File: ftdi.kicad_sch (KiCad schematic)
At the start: 31 parts, among them U1001 AT93C56, U1002 FT2232HL, Y1001 12MHz

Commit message: Schematic sketching done
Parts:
- R1001, R1002, R1005, R1006, R1007, R1008, R1009, R1010, R1011: Tolerance (none) -> 5%
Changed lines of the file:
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@@
+      (effects (font (size 1.27 1.27)) hide)
+    )
+    (property "Tolerance" "5%" (id 4) (at 38.1 44.45 0)
       (effects (font (size 1.27 1.27)) hide)
     )
@@
     )
     (property "Datasheet" "~" (id 3) (at 38.1 57.15 0)
+      (effects (font (size 1.27 1.27)) hide)
+    )
+    (property "Tolerance" "5%" (id 4) (at 38.1 57.15 0)
       (effects (font (size 1.27 1.27)) hide)
     )
@@
       (effects (font (size 1.27 1.27)) hide)
     )
+    (property "Tolerance" "5%" (id 4) (at 83.82 123.19 0)
+      (effects (font (size 1.27 1.27)) hide)
+    )
     (pin "1")
     (pin "2")
@@
       (effects (font (size 1.27 1.27)) hide)
     )
+    (property "Tolerance" "5%" (id 4) (at 83.82 101.6 0)
+      (effects (font (size 1.27 1.27)) hide)
+    )
     (pin "1")
     (pin "2")
@@
     )
     (property "Datasheet" "~" (id 3) (at 91.44 101.6 0)
+      (effects (font (size 1.27 1.27)) hide)
+    )
+    (property "Tolerance" "5%" (id 4) (at 91.44 101.6 0)
       (effects (font (size 1.27 1.27)) hide)
     )
@@
       (effects (font (size 1.27 1.27)) hide)
     )
+    (property "Tolerance" "5%" (id 4) (at 101.6 96.52 0)
+      (effects (font (size 1.27 1.27)) hide)
+    )
     (pin "1")
     (pin "2")
@@
     )
     (property "Datasheet" "~" (id 3) (at 95.25 85.09 0)
+      (effects (font (size 1.27 1.27)) hide)
+    )
+    (property "Tolerance" "5%" (id 4) (at 95.25 85.09 0)
       (effects (font (size 1.27 1.27)) hide)
     )
@@
       (effects (font (size 1.27 1.27)) hide)
     )
+    (property "Tolerance" "5%" (id 4) (at 76.2 101.6 0)
+      (effects (font (size 1.27 1.27)) hide)
+    )
     (pin "1")
     (pin "2")
@@
       (effects (font (size 1.27 1.27)) hide)
     )
+    (property "Tolerance" "5%" (id 4) (at 177.8 125.73 0)
+      (effects (font (size 1.27 1.27)) hide)
+    )

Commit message: Update schematic layout, separate into sheets
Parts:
- renumbered C1001 to C1301, C1002 to C1302, C1003 to C1303, C1004 to C1304, C1005 to C1305, C1006 to C1306, C1007 to C1307, C1008 to C1308, C1009 to C1309, C1010 to C1310, C1011 to C1311, C1012 to C1312, C1013 to C1313, C1014 to C1314, D1001 to D1301, FB1001 to FB1301, FB1002 to FB1302, R1001 to R1301, R1002 to R1302, R1003 to R1303, R1004 to R1304, R1005 to R1305, R1006 to R1306, R1007 to R1307, R1008 to R1308, R1009 to R1309, R1010 to R1310, R1011 to R1311, U1001 to U1301, U1002 to U1302, Y1001 to Y1301
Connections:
- net CDONE renamed IOB.CDONE
- net IO1 renamed IOB.IO1
- net IO2 renamed IOB.IO2
- net ~{CRESET} renamed IOB.~{CRESET}

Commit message: Schematic update
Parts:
- C1301, C1302: Spec1 (none) -> 25V; Spec2 (none) -> C0G; Tolerance (none) -> 10%
- C1303, C1304, C1305, C1306, C1307, C1308, C1309, C1310, C1311, C1312, C1313, C1314: Spec1 (none) -> 16V; Spec2 (none) -> X5R; Tolerance (none) -> 20%
- R1307: value 2.2k -> 2.4k
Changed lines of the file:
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@@
+      (effects (font (size 1.27 1.27)) hide)
+    )
+    (property "Spec1" "16V" (id 4) (at 254 76.2 0)
+      (effects (font (size 1.27 1.27)) hide)
+    )
+    (property "Spec2" "X5R" (id 5) (at 254 76.2 0)
+      (effects (font (size 1.27 1.27)) hide)
+    )
+    (property "Tolerance" "20%" (id 6) (at 254 76.2 0)
       (effects (font (size 1.27 1.27)) hide)
     )
@@
     )
     (property "Datasheet" "~" (id 3) (at 241.3 76.2 0)
+      (effects (font (size 1.27 1.27)) hide)
+    )
+    (property "Spec1" "16V" (id 4) (at 241.3 76.2 0)
+      (effects (font (size 1.27 1.27)) hide)
+    )
+    (property "Spec2" "X5R" (id 5) (at 241.3 76.2 0)
+      (effects (font (size 1.27 1.27)) hide)
+    )
+    (property "Tolerance" "20%" (id 6) (at 241.3 76.2 0)
       (effects (font (size 1.27 1.27)) hide)
     )
@@
       (effects (font (size 1.27 1.27)) hide)
     )
+    (property "Spec1" "16V" (id 4) (at 266.7 44.45 0)
+      (effects (font (size 1.27 1.27)) hide)
+    )
+    (property "Spec2" "X5R" (id 5) (at 266.7 44.45 0)
+      (effects (font (size 1.27 1.27)) hide)
+    )
+    (property "Tolerance" "20%" (id 6) (at 266.7 44.45 0)
+      (effects (font (size 1.27 1.27)) hide)
+    )
     (pin "1")
     (pin "2")
@@
     )
     (property "Datasheet" "~" (id 3) (at 241.3 139.7 0)
+      (effects (font (size 1.27 1.27)) hide)
+    )
+    (property "Spec1" "16V" (id 4) (at 241.3 139.7 0)
+      (effects (font (size 1.27 1.27)) hide)
+    )
+    (property "Spec2" "X5R" (id 5) (at 241.3 139.7 0)
+      (effects (font (size 1.27 1.27)) hide)
+    )
+    (property "Tolerance" "20%" (id 6) (at 241.3 139.7 0)
       (effects (font (size 1.27 1.27)) hide)
     )
@@
       (effects (font (size 1.27 1.27)) hide)
     )
+    (property "Spec1" "16V" (id 4) (at 241.3 44.45 0)
+      (effects (font (size 1.27 1.27)) hide)
+    )
+    (property "Spec2" "X5R" (id 5) (at 241.3 44.45 0)
+      (effects (font (size 1.27 1.27)) hide)
+    )
+    (property "Tolerance" "20%" (id 6) (at 241.3 44.45 0)
+      (effects (font (size 1.27 1.27)) hide)
+    )
     (pin "1")
     (pin "2")
@@
     )
     (property "Datasheet" "~" (id 3) (at 76.2 151.13 0)
+      (effects (font (size 1.27 1.27)) hide)
+    )
+    (property "Spec1" "25V" (id 4) (at 76.2 151.13 0)
+      (effects (font (size 1.27 1.27)) hide)
+    )
+    (property "Spec2" "C0G" (id 5) (at 76.2 151.13 0)
+      (effects (font (size 1.27 1.27)) hide)
+    )
+    (property "Tolerance" "10%" (id 6) (at 76.2 151.13 0)
       (effects (font (size 1.27 1.27)) hide)
     )
@@
       (effects (font (size 1.27 1.27)) hide)
     )
+    (property "Spec1" "16V" (id 4) (at 254 139.7 0)
+      (effects (font (size 1.27 1.27)) hide)
+    )
+    (property "Spec2" "X5R" (id 5) (at 254 139.7 0)
+      (effects (font (size 1.27 1.27)) hide)
+    )
+    (property "Tolerance" "20%" (id 6) (at 254 139.7 0)
+      (effects (font (size 1.27 1.27)) hide)
+    )
     (pin "1")
     (pin "2")
@@
     (in_bom yes) (on_board yes) (fields_autoplaced)
     (property "Reference" "R1307" (id 0) (at 83.82 126.3555 90))
-    (property "Value" "2.2k" (id 1) (at 83.82 129.1306 90))
+    (property "Value" "2.4k" (id 1) (at 83.82 129.1306 90))
     (property "Footprint" "Resistor_SMD:R_0805_2012Metric" (id 2) (at 83.82 121.412 90)
       (effects (font (size 1.27 1.27)) hide)
@@
     )
     (property "Datasheet" "~" (id 3) (at 228.6 139.7 0)
+      (effects (font (size 1.27 1.27)) hide)
+    )
+    (property "Spec1" "16V" (id 4) (at 228.6 139.7 0)
+      (effects (font (size 1.27 1.27)) hide)
+    )
+    (property "Spec2" "X5R" (id 5) (at 228.6 139.7 0)
+      (effects (font (size 1.27 1.27)) hide)
+    )
+    (property "Tolerance" "20%" (id 6) (at 228.6 139.7 0)
       (effects (font (size 1.27 1.27)) hide)
     )
@@
       (effects (font (size 1.27 1.27)) hide)
     )
+    (property "Spec1" "16V" (id 4) (at 228.6 44.45 0)
+      (effects (font (size 1.27 1.27)) hide)
+    )
+    (property "Spec2" "X5R" (id 5) (at 228.6 44.45 0)
+      (effects (font (size 1.27 1.27)) hide)
+    )
+    (property "Tolerance" "20%" (id 6) (at 228.6 44.45 0)
+      (effects (font (size 1.27 1.27)) hide)
+    )
     (pin "1")
     (pin "2")
@@
       (effects (font (size 1.27 1.27)) hide)
     )
+    (property "Spec1" "16V" (id 4) (at 254 107.95 0)
+      (effects (font (size 1.27 1.27)) hide)
+    )
+    (property "Spec2" "X5R" (id 5) (at 254 107.95 0)
+      (effects (font (size 1.27 1.27)) hide)
+    )
+    (property "Tolerance" "20%" (id 6) (at 254 107.95 0)
+      (effects (font (size 1.27 1.27)) hide)
+    )
     (pin "1")
     (pin "2")
@@
     )
     (property "Datasheet" "~" (id 3) (at 266.7 139.7 0)
+      (effects (font (size 1.27 1.27)) hide)
+    )
+    (property "Spec1" "16V" (id 4) (at 266.7 139.7 0)
+      (effects (font (size 1.27 1.27)) hide)
+    )
+    (property "Spec2" "X5R" (id 5) (at 266.7 139.7 0)
+      (effects (font (size 1.27 1.27)) hide)
+    )
+    (property "Tolerance" "20%" (id 6) (at 266.7 139.7 0)
       (effects (font (size 1.27 1.27)) hide)
     )
@@
       (effects (font (size 1.27 1.27)) hide)
     )
+    (property "Spec1" "16V" (id 4) (at 241.3 107.95 0)
+      (effects (font (size 1.27 1.27)) hide)
+    )
+    (property "Spec2" "X5R" (id 5) (at 241.3 107.95 0)
+      (effects (font (size 1.27 1.27)) hide)
+    )
+    (property "Tolerance" "20%" (id 6) (at 241.3 107.95 0)
+      (effects (font (size 1.27 1.27)) hide)
+    )
     (pin "1")
     (pin "2")
@@
       (effects (font (size 1.27 1.27)) hide)
     )
+    (property "Spec1" "25V" (id 4) (at 99.06 151.13 0)
+      (effects (font (size 1.27 1.27)) hide)
+    )
+    (property "Spec2" "C0G" (id 5) (at 99.06 151.13 0)
+      (effects (font (size 1.27 1.27)) hide)
+    )
+    (property "Tolerance" "10%" (id 6) (at 99.06 151.13 0)
+      (effects (font (size 1.27 1.27)) hide)
+    )
     (pin "1")
     (pin "2")
@@
       (effects (font (size 1.27 1.27)) hide)
     )
+    (property "Spec1" "16V" (id 4) (at 254 44.45 0)
+      (effects (font (size 1.27 1.27)) hide)
+    )
+    (property "Spec2" "X5R" (id 5) (at 254 44.45 0)
+      (effects (font (size 1.27 1.27)) hide)
+    )
+    (property "Tolerance" "20%" (id 6) (at 254 44.45 0)
+      (effects (font (size 1.27 1.27)) hide)
+    )

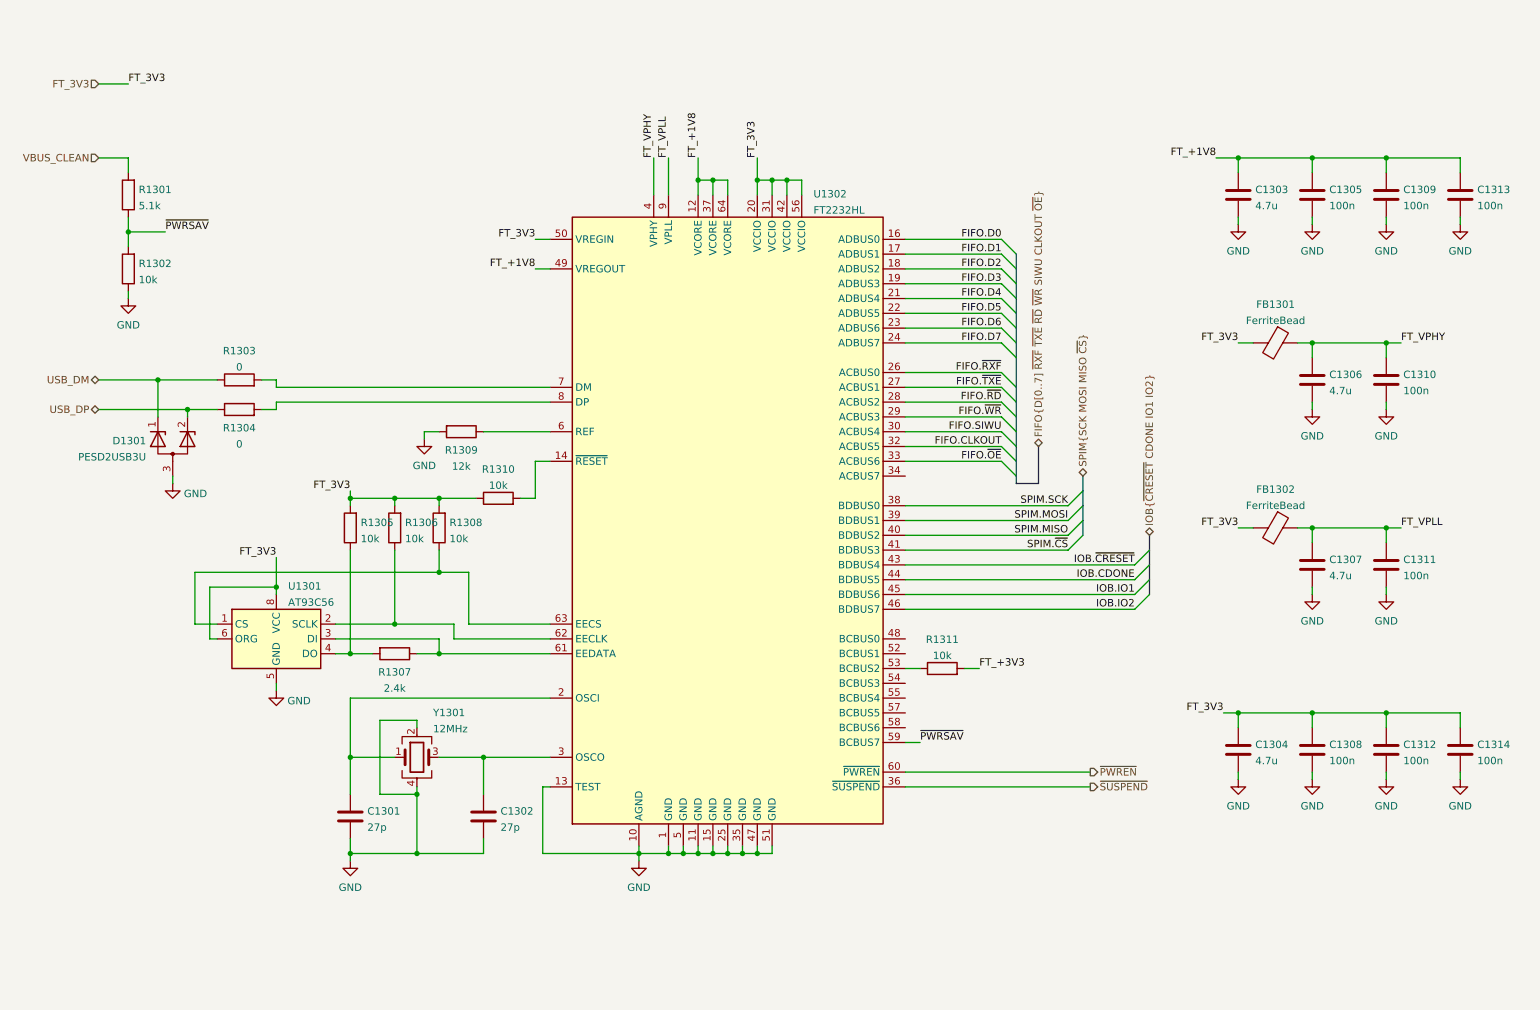
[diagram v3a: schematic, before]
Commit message: Schematic: better LDO output capacitor selection, clarified BOM
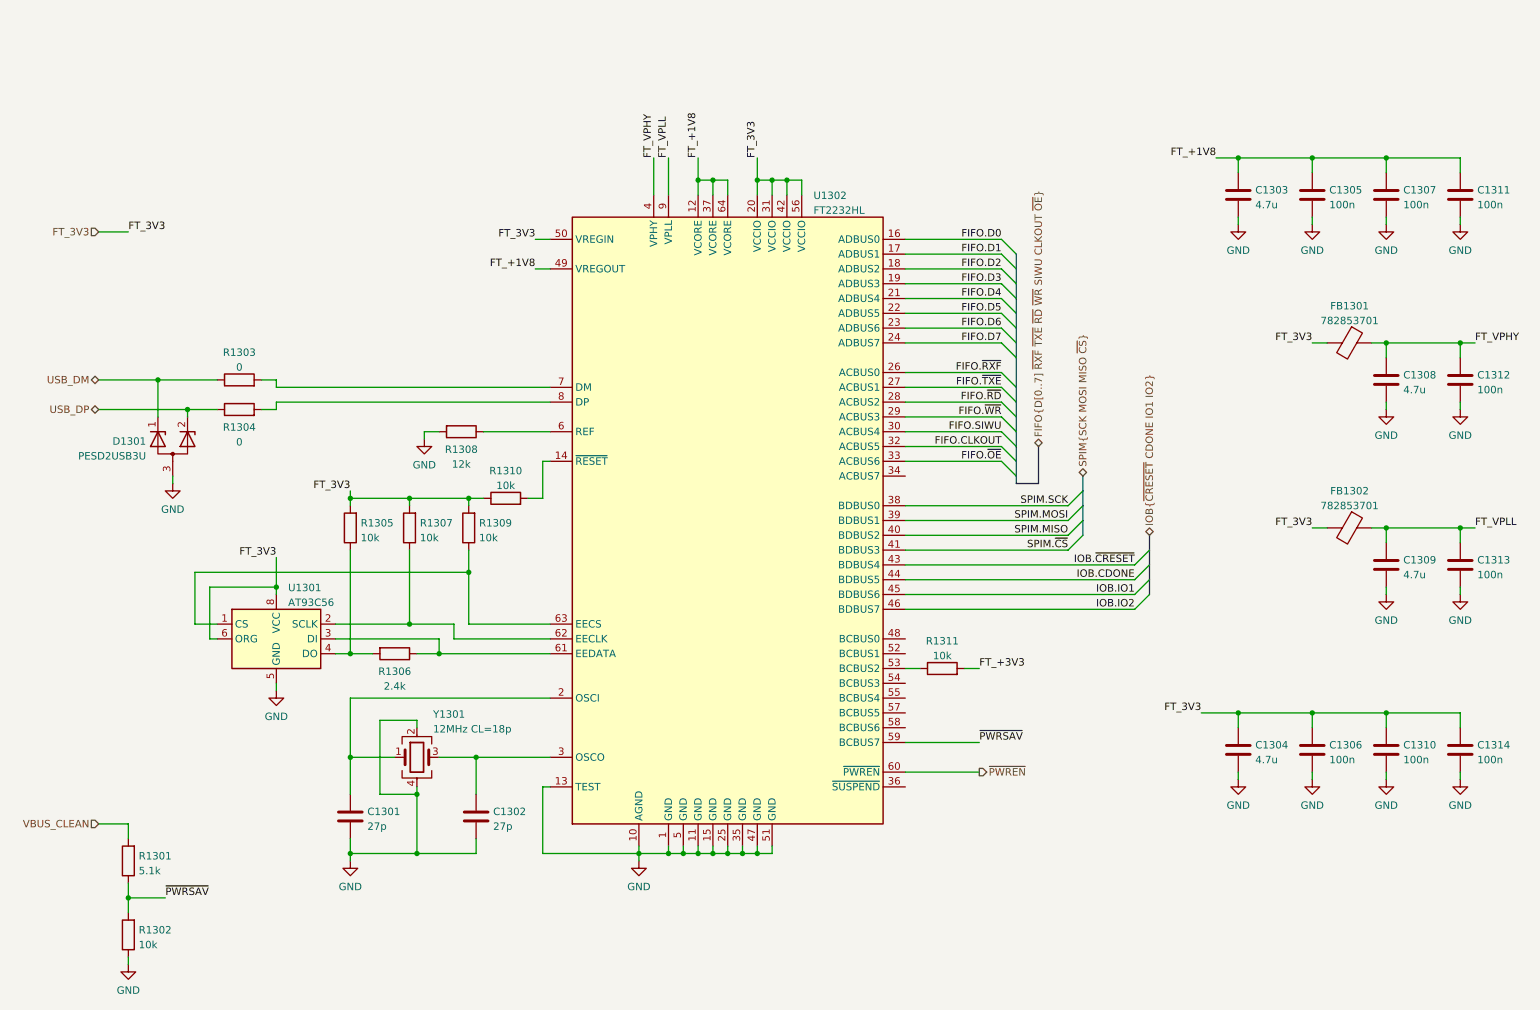
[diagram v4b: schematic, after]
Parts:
- C1303, C1304, C1305, C1314: Spec1 16V -> (none); Spec2 X5R -> (none); Tolerance 20% -> (none)
- C1306: renamed from C1308; Spec1 16V -> (none); Spec2 X5R -> (none); Tolerance 20% -> (none)
- C1307: renamed from C1309; Spec1 16V -> (none); Spec2 X5R -> (none); Tolerance 20% -> (none)
- C1308: renamed from C1306; Spec1 16V -> (none); Spec2 X5R -> (none); Tolerance 20% -> (none)
- C1309: renamed from C1307; Spec1 16V -> (none); Spec2 X5R -> (none); Tolerance 20% -> (none)
- C1310: renamed from C1312; Spec1 16V -> (none); Spec2 X5R -> (none); Tolerance 20% -> (none)
- C1311: renamed from C1313; Spec1 16V -> (none); Spec2 X5R -> (none); Tolerance 20% -> (none)
- C1312: renamed from C1310; Spec1 16V -> (none); Spec2 X5R -> (none); Tolerance 20% -> (none)
- C1313: renamed from C1311; Spec1 16V -> (none); Spec2 X5R -> (none); Tolerance 20% -> (none)
- FB1301, FB1302: value FerriteBead -> 782853701; footprint (none) -> Inductor_SMD:L_0805_2012Metric_Pad1.05x1.20mm_HandSolder
- Y1301: value 12MHz -> 12MHz CL=18p
- renumbered R1307 to R1306, R1306 to R1307, R1309 to R1308, R1308 to R1309
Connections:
- net ~{SUSPEND}: no longer names the net of U1302.36 (~{SUSPEND})
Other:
- moved on the sheet: C1302, C1308, C1309, C1312, C1313, FB1301, FB1302, R1301, R1302, R1307, R1309, R1310

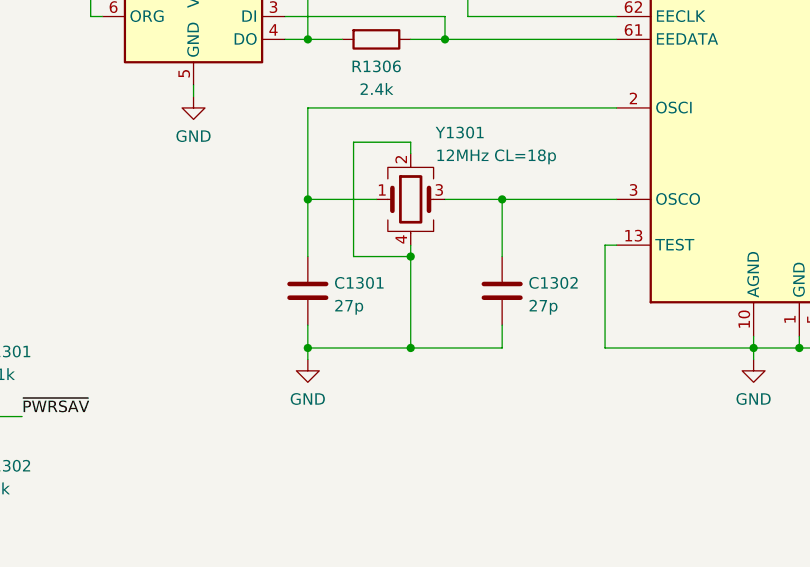
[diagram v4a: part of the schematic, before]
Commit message: Schematic: yet another update -Improve way caps are specified once again -Update cap voltages based on ESD simulation -Make anti-aliasing LC filter more practical - with much less inductors -Specify Mfr & MfrPN for almost all components (most from Mouser, some from Digikey)
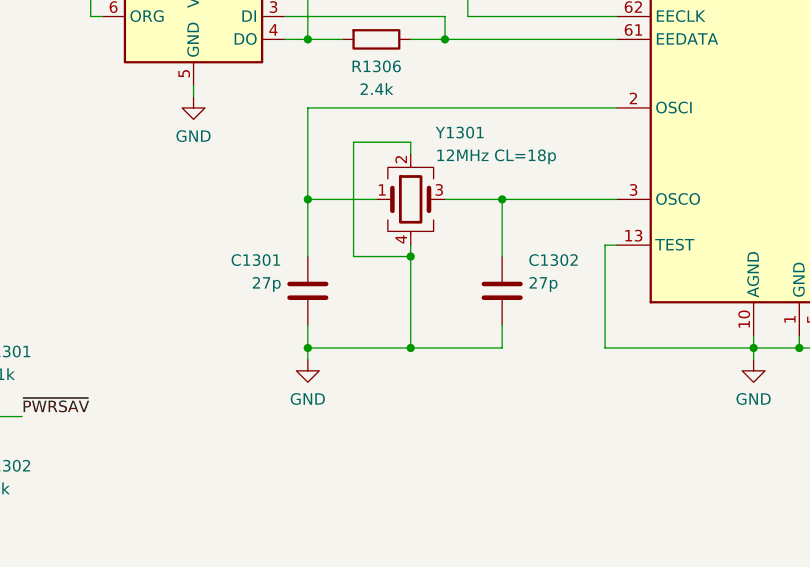
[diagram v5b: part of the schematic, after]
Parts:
- C1301, C1302: Mfr (none) -> YAGEO; Mfr PN (none) -> CC0805JRNPO9BN270; Spec1 25V -> (none); Spec2 C0G -> (none); Tolerance 10% -> (none)
- C1303, C1304, C1308, C1309: Mfr (none) -> Murata; Mfr PN (none) -> GRM21BR71C475ME51
- C1305, C1306, C1307, C1310, C1311, C1312, C1313, C1314: Mfr (none) -> Samsung; Mfr PN (none) -> CL21B104KBFNNNE
- D1301: footprint (none) -> Package_TO_SOT_SMD:SOT-23; Mfr (none) -> Nexperia; Mfr PN (none) -> PESD2USB3UV
- FB1301, FB1302: Mfr (none) -> Wurth; Mfr PN (none) -> 782853701
- R1301, R1302, R1305, R1306, R1307, R1308, R1309, R1310, R1311: Tolerance 5% -> (none)
- U1301: footprint Package_SO:SOIC-8_3.9x4.9mm_P1.27mm -> Package_SO:TSSOP-8_4.4x3mm_P0.65mm; Mfr (none) -> Microchip; Mfr PN (none) -> AT93C56B-XHM-T
- U1302: Mfr (none) -> FTDI; Mfr PN (none) -> FT2232HL
- Y1301: Mfr (none) -> ECS; Mfr PN (none) -> ECS-120-18-33-JGN-TR3
